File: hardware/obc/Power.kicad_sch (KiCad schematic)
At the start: 50 parts, among them Q401 MBT2222ADW1T1, Q402 MBT2222ADW1T1, Q403 IRLML2803, Q404 IRF7406PbF, U401 TPS7A4501DCQT, U403 TPS54226PWPRPWP14_2P31X2P46-L, U404 ADM1176-1ARMZ-R7, U405 BQ25886RGER

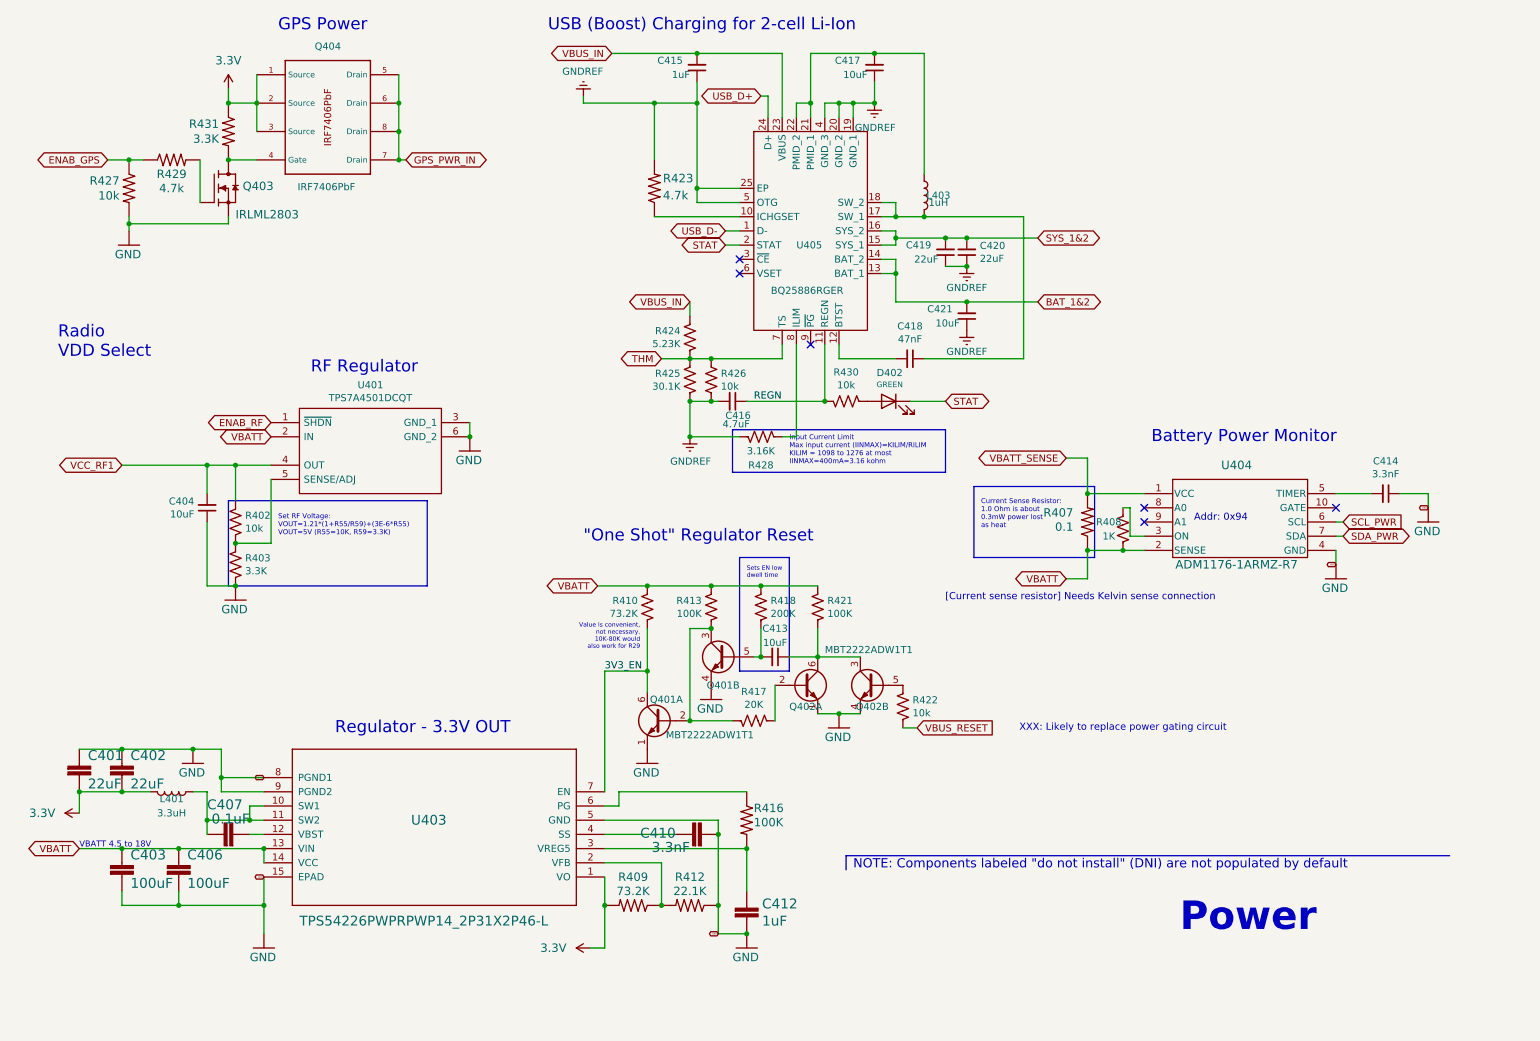
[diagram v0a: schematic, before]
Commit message: OBC: Continuing work towards the next revision
- Cleaned up text on Avionics Page
- Changed some descriptions and cleaned up text on Power Page
- Changed Power Relay A schematic to one from PCB
- Changed R120 and R401 changed from 107k to 34.8k and changed R121 and R404 from 0 to 10k and R127 and R419 from 3.01k to 3.83k (Solar Chargers Page)
- Checked R303 and R304 resistor value and believe 27 is correct
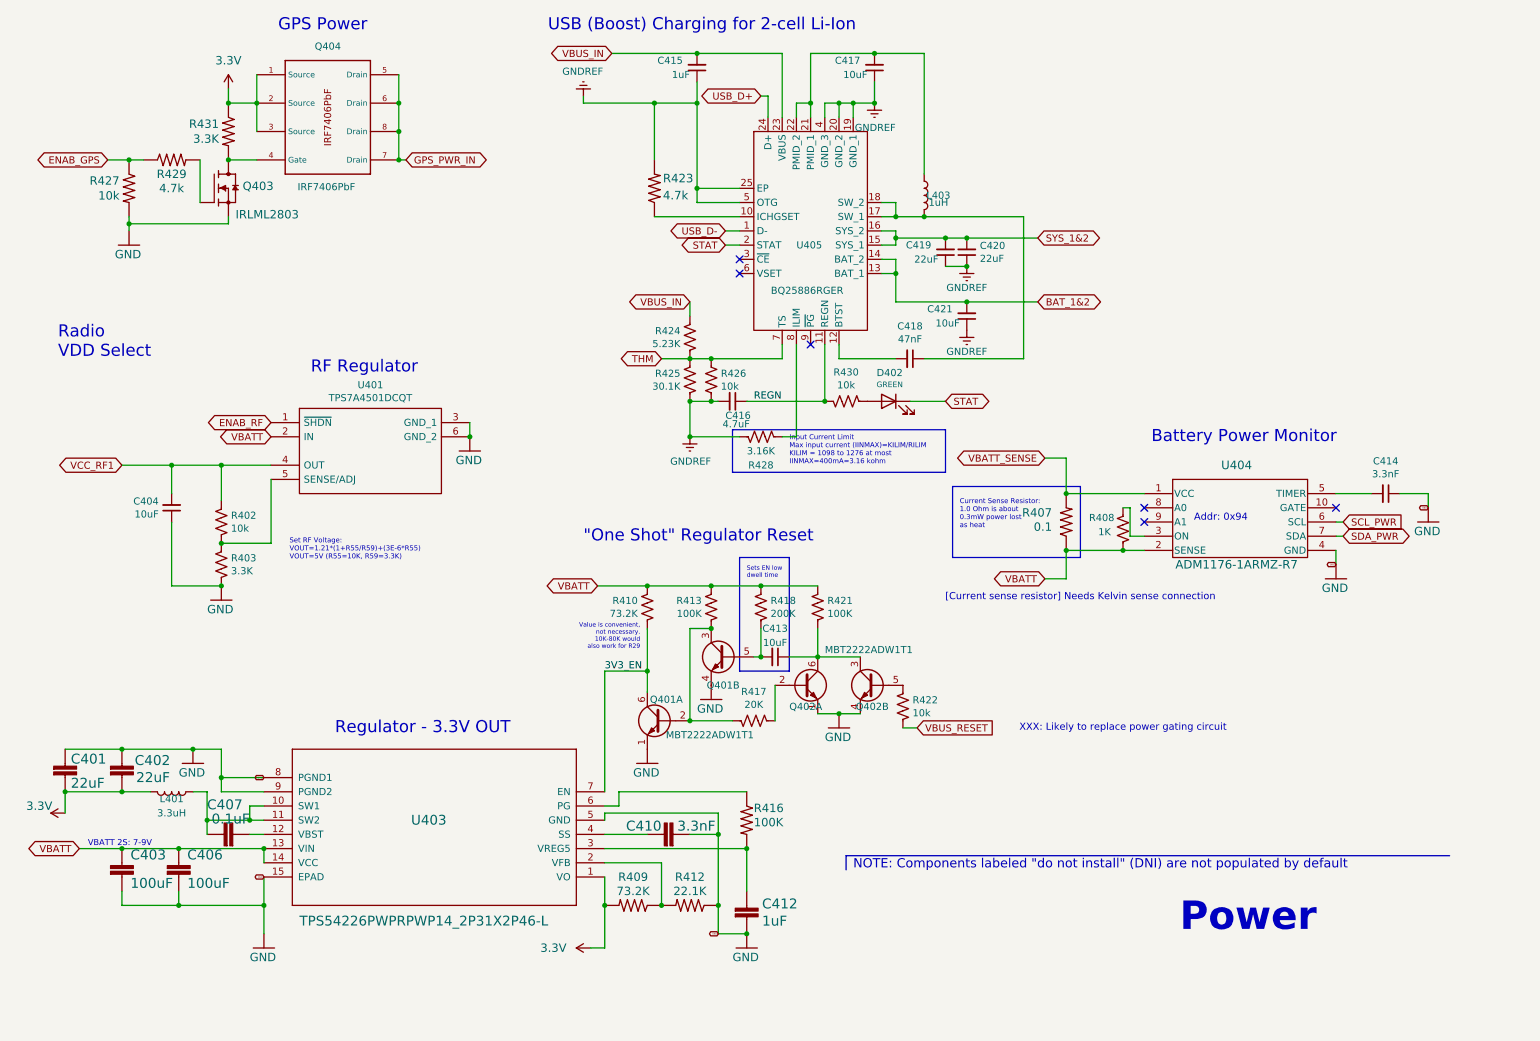
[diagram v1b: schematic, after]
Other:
- note added: "VBATT 2S: 7-9V"
- note removed: "VBATT 4.5 to 18V"
- moved on the sheet: C401, C404, C410, R402, R403, R407

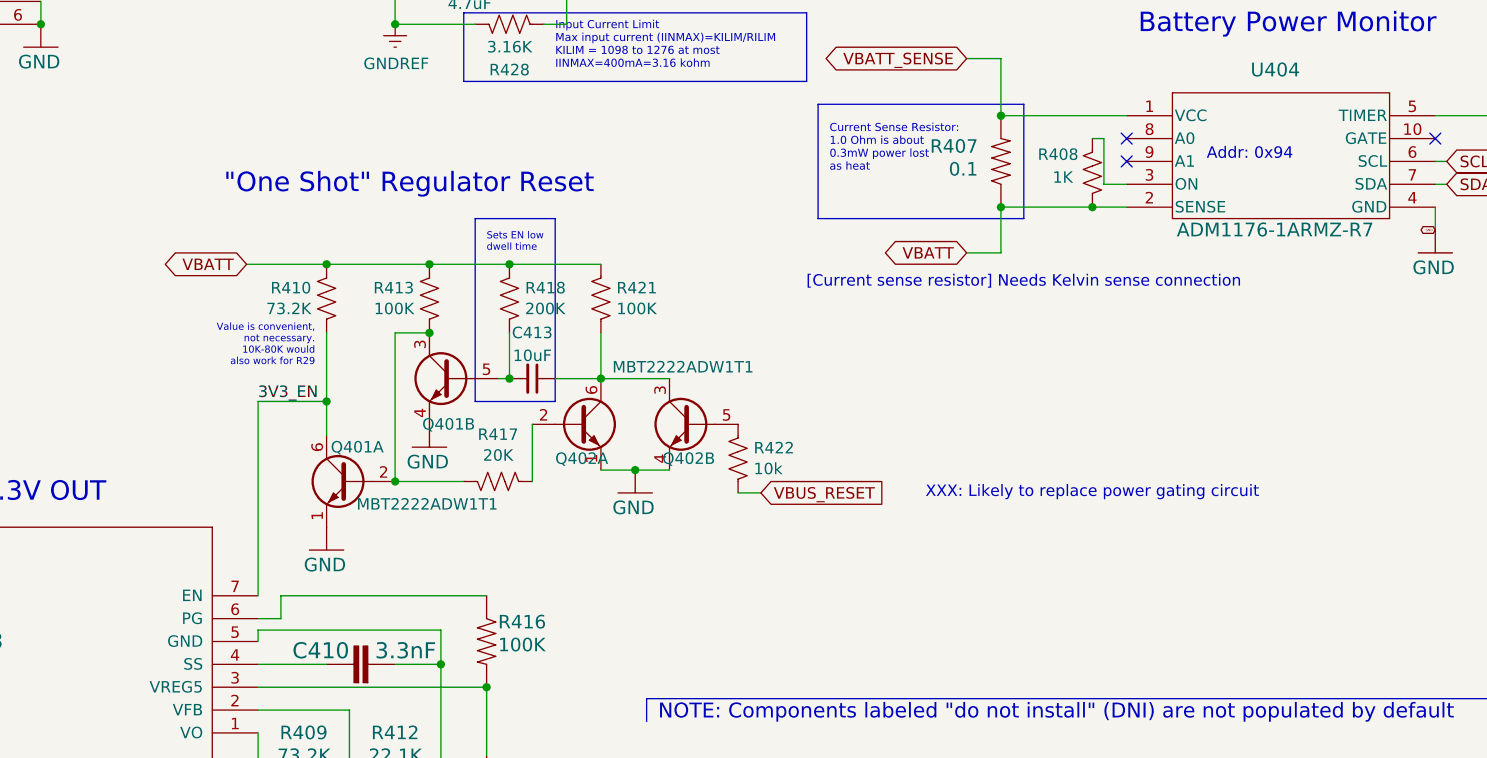
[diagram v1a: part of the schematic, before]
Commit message: OBC: Added new power supervisor and watch dog circuit
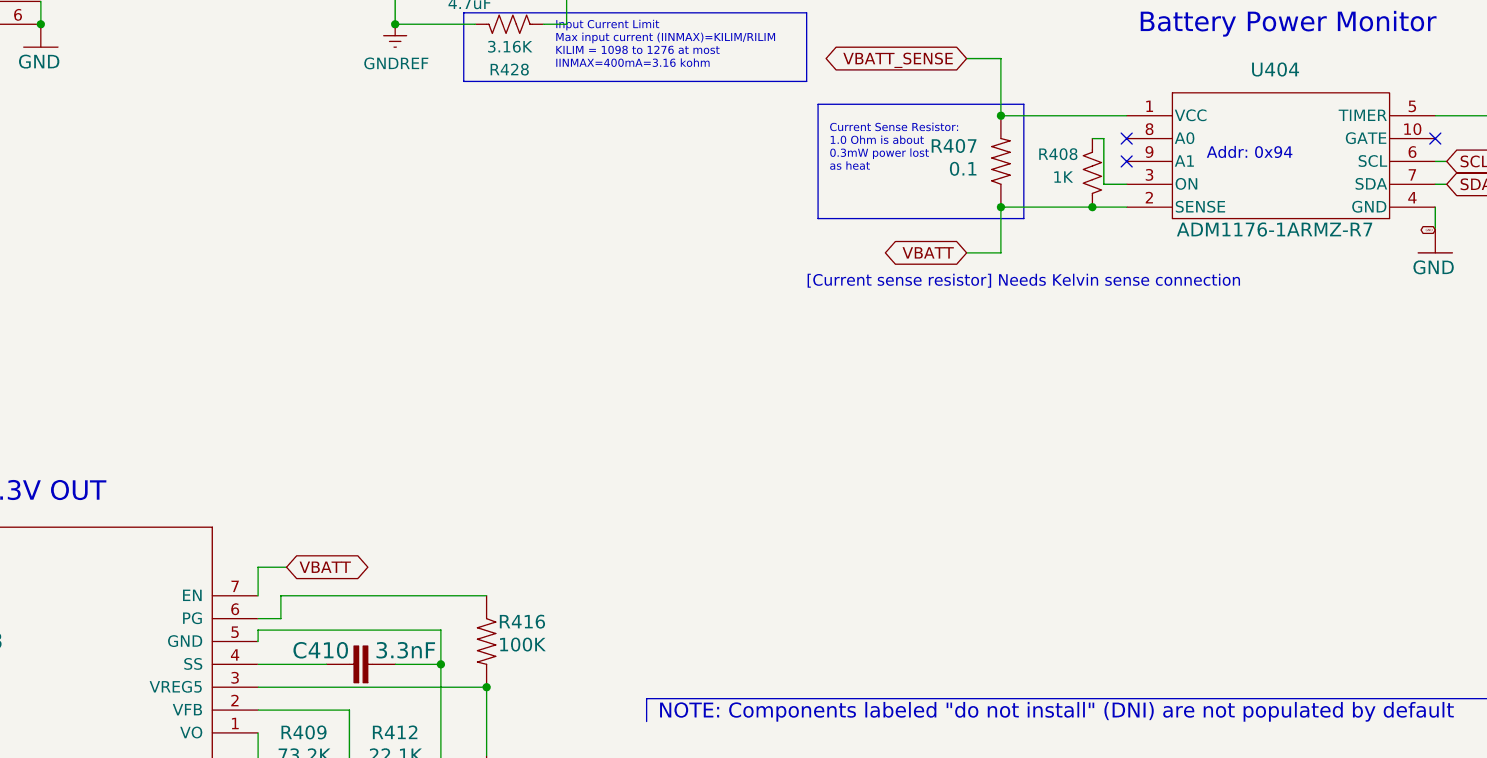
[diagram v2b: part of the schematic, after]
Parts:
- removed C413: 10uF, Capacitor_SMD:C_0603_1608Metric, symbol Device:C_Small
- removed Q401, Q402: MBT2222ADW1T1, Package_TO_SOT_SMD:SOT-363_SC-70-6, symbol Transistor_BJT:MBT2222ADW1T1
- removed R410: 73.2K, Resistor_SMD:R_0603_1608Metric, symbol Device:R_US
- removed R413, R421: 100K, Resistor_SMD:R_0603_1608Metric, symbol Device:R_US
- removed R417: 20K, Resistor_SMD:R_0603_1608Metric, symbol Device:R_US
- removed R418: 200K, Resistor_SMD:R_0603_1608Metric, symbol Device:R_US
- removed R422: 10k, Resistor_SMD:R_0603_1608Metric, symbol Device:R_US
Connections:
- net 3V3_EN is gone; now on net VBATT: U403.7 (EN)
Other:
- note removed: ""One Shot" Regulator Reset"
- note removed: "Sets EN low dwell time"
- note removed: "Value is convenient, not necessary. 10K-80K would also work for R29"
- note removed: "XXX: Likely to replace power gating circuit"

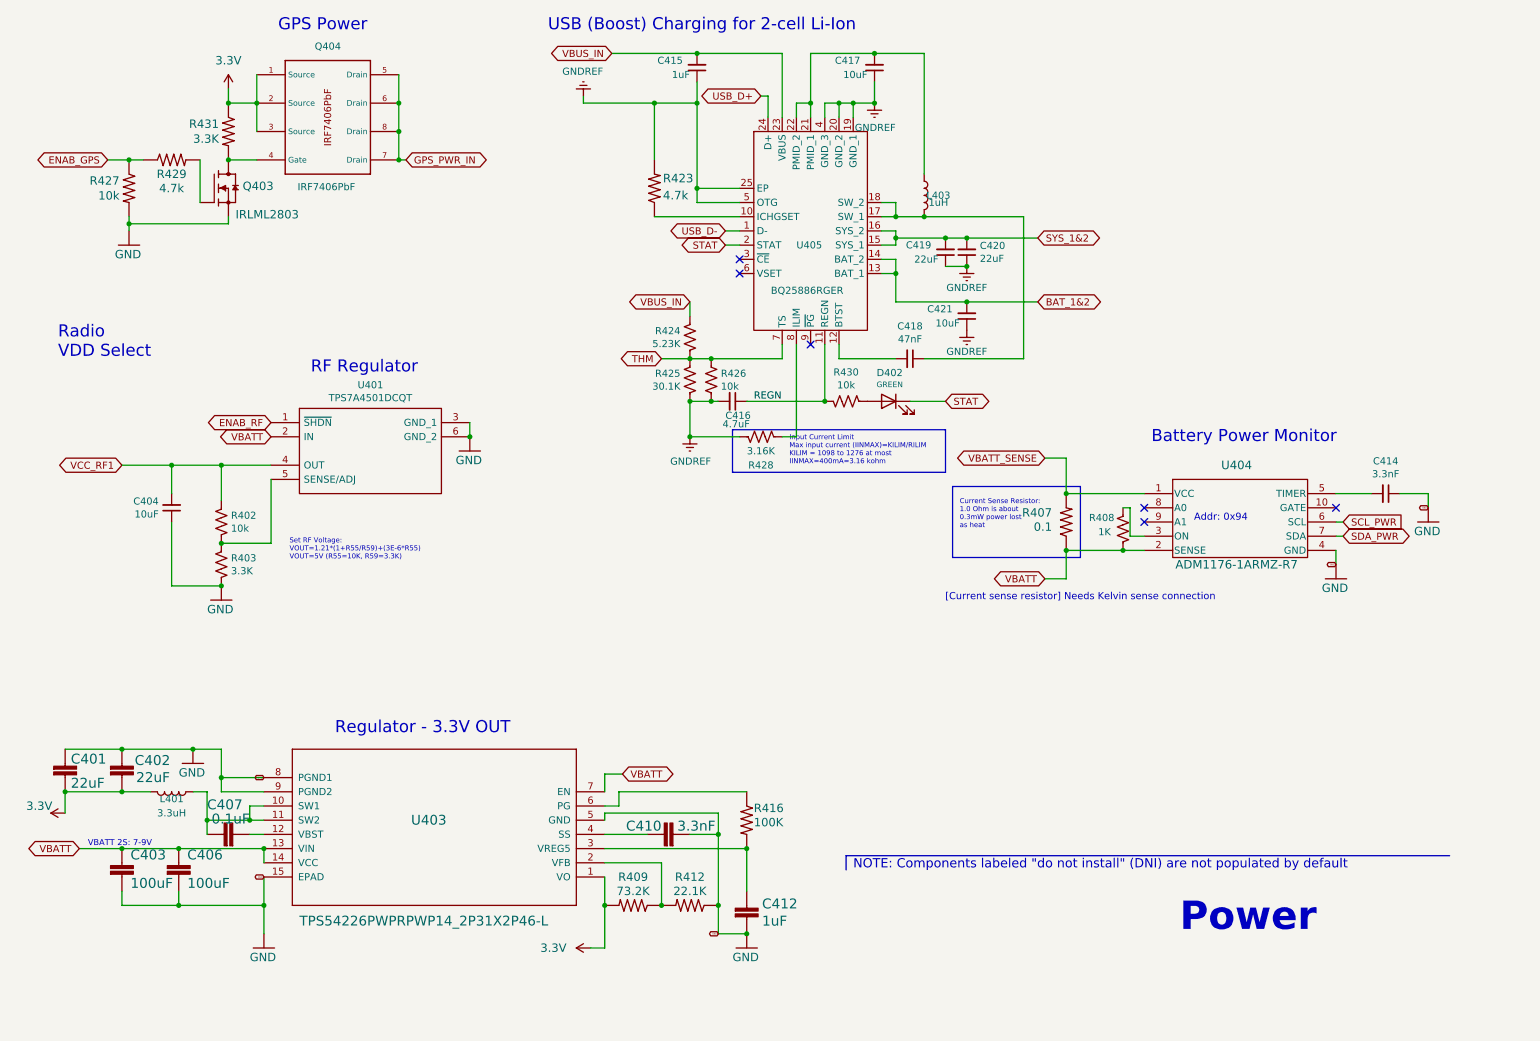
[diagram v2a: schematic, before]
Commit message: obc: power sup: fix mistake, add theory, clean up
1. During component selection, FET drain and sources were reversed
   (fixed).
2. Was able to make page much cleaner.
3. Rearrange power page, add some XXX comments.
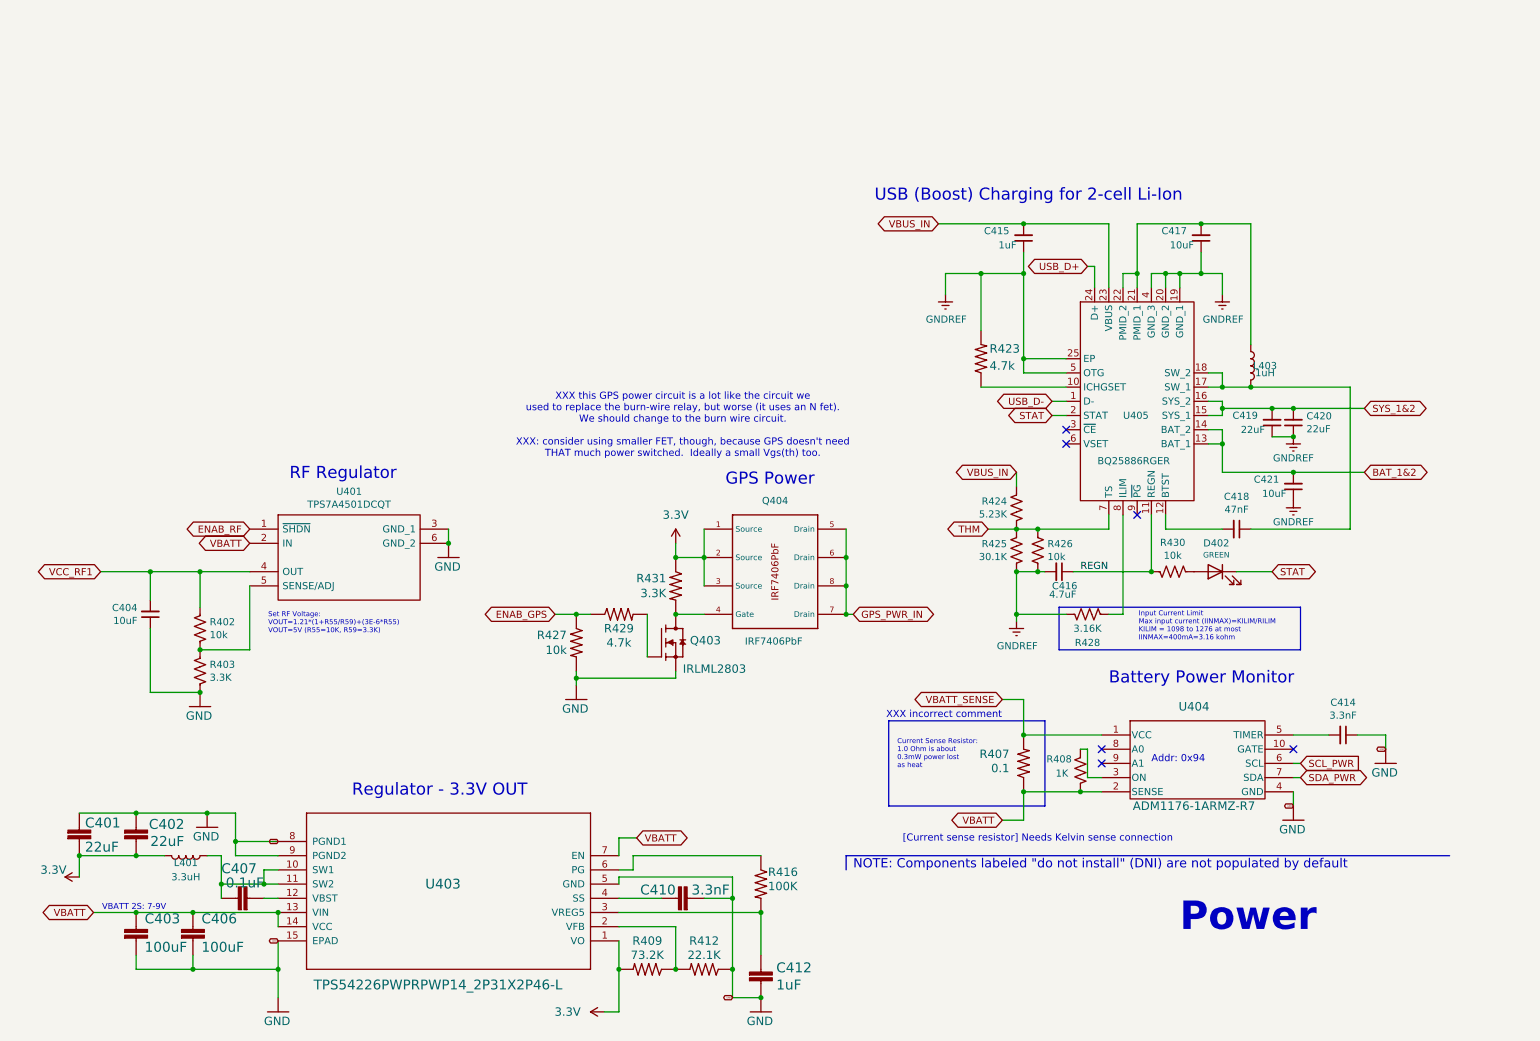
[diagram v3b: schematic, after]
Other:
- note added: "XXX incorrect comment"
- note added: "XXX this GPS power circuit is a lot like the circuit we used to replace the burn-wire relay, but worse (it uses an N fet). We should change to the burn wire circuit. XXX: consider using smaller FET, though, because GPS doesn't need THAT much power switched. Ideally a small Vgs(th) too."
- note removed: "Radio VDD Select"
- moved on the sheet: C401, C402, C403, C404, C406, C407, C410, C412, C414, C415, C416, C417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
